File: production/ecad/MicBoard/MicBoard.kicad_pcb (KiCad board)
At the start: 2 copper layers, 50.8 x 38.1 mm, 25 parts, among them J1 Conn_01x03_Pin, J2 532610771, U2 OPA1671IDBVR

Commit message: fix drc errors
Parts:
- added TP3: TestPoint, TestPoint:TestPoint_Pad_D1.0mm, F.Cu at (77.7, 61.6)
- moved TP1 35.7 mm to (60.1, 84.7)
- moved TP2 14.4 mm to (72.4, 70.9)
- moved R3 1.43 mm to (68.1, 71.0)
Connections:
- R1 pad 2: +3.3V -> +3V3
- U2 pad 5: +3.3V -> +3V3
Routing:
- net Net-(U2-OUT): track 28.2 -> 59.6 mm
- net Net-(U2-+IN): track 13.5 -> 41.3 mm
- net GND: track 45.2 -> 54.3 mm, vias 12 -> 14
- net +3V3: track 12.9 -> 17.9 mm, vias 4 -> 5
- net +3.3V: track 2.63 -> 0.00 mm, vias 1 -> 0
- added copper zone on F.Cu, net +3V3
- added copper zone on B.Cu, net GND

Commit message: more drc fixes
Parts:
- moved TP2 8.05 mm to (64.4, 70.0)
- moved R6 7.55 mm to (72.2, 70.7), turned to 0 degrees
- moved R3 1.76 mm to (67.9, 69.2), turned to -90 degrees
- moved C2 0.25 mm to (67.5, 61.7)
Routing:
- net Net-(U2-OUT): track 59.6 -> 42.9 mm
- net Net-(U2--IN): track 38.7 -> 35.7 mm
- net Net-(C2-Pad1): track 18.8 -> 19.8 mm
- net Net-(U2-+IN): track 41.3 -> 40.3 mm

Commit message: more fixes to layout
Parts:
- moved R2 9.09 mm to (66.5, 56.2), turned to -90 degrees
- moved C10 8.74 mm to (89.9, 75.2)
- moved C9 8.74 mm to (85.3, 75.2)
- moved R6 7.87 mm to (66.6, 76.2)
- moved C2 5.62 mm to (64.3, 66.4), turned to -90 degrees
- moved TP2 4.90 mm to (68.6, 67.4), turned to 180 degrees
- moved R3 3.93 mm to (64.3, 70.8)
- moved R4 2.69 mm to (71.8, 56.2)
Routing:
- net Net-(U2-+IN): track 40.3 -> 23.5 mm
- net Net-(C1-Pad1): track 27.4 -> 17.1 mm
- net +3V3: track 17.9 -> 10.7 mm, vias 5 -> 2
- net Net-(U3-GSEL): track 11.9 -> 5.37 mm
- net Net-(U2-OUT): track 42.9 -> 47.9 mm
- net Net-(U2--IN): track 35.7 -> 38.5 mm
- net Net-(C2-Pad1): track 19.8 -> 18.0 mm
- net Net-(U3-REGO): track 7.94 -> 6.32 mm
- net GND: track 54.2 -> 54.7 mm
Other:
- outline, holes or cut-outs redrawn

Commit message: ground mounting holes
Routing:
- net GND: vias 14 -> 18
- net (no net): vias 4 -> 0
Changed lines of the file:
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@@
   (gr_circle (center 97.79 54.609998) (end 99.06 52.832)
     (stroke (width 0.1) (type default)) (fill none) (layer "Edge.Cuts"))
-  (via (at 54.61 54.61) (size 4.318) (drill 3.7973) (layers "F.Cu" "B.Cu") (net 0))
-  (via (at 97.79 54.61) (size 4.318) (drill 3.7973) (layers "F.Cu" "B.Cu") (net 0))
-  (via (at 54.61 85.09) (size 4.318) (drill 3.7973) (layers "F.Cu" "B.Cu") (net 0))
-  (via (at 97.79 85.09) (size 4.318) (drill 3.7973) (layers "F.Cu" "B.Cu") (net 0))
   (segment (start 71.708 55.278) (end 71.755 55.325) (width 0.25) (layer "F.Cu") (net 1))
   (segment (start 60.786 57.357) (end 60.786 53.467) (width 0.25) (layer "F.Cu") (net 1))
@@
   (segment (start 86.294 76.83) (end 86.294 75.184) (width 0.25) (layer "F.Cu") (net 2))
   (segment (start 55.118 80.01) (end 53.086 80.01) (width 0.25) (layer "F.Cu") (net 2))
+  (via (at 54.61 54.61) (size 4.318) (drill 3.7973) (layers "F.Cu" "B.Cu") (free) (net 2))
+  (via (at 97.79 54.61) (size 4.318) (drill 3.7973) (layers "F.Cu" "B.Cu") (free) (net 2))
   (via (at 92.837 65.278) (size 0.8) (drill 0.4) (layers "F.Cu" "B.Cu") (free) (net 2))
   (via (at 70.104 64.516) (size 0.8) (drill 0.4) (layers "F.Cu" "B.Cu") (net 2))
+  (via (at 54.61 85.09) (size 4.318) (drill 3.7973) (layers "F.Cu" "B.Cu") (free) (net 2))
   (via (at 97.155 78.486) (size 0.8) (drill 0.4) (layers "F.Cu" "B.Cu") (free) (net 2))
   (via (at 86.934 77.47) (size 0.8) (drill 0.4) (layers "F.Cu" "B.Cu") (free) (net 2))
@@
   (via (at 52.959 80.137) (size 0.8) (drill 0.4) (layers "F.Cu" "B.Cu") (free) (net 2))
   (via (at 80.137 58.547) (size 0.8) (drill 0.4) (layers "F.Cu" "B.Cu") (free) (net 2))
+  (via (at 97.79 85.09) (size 4.318) (drill 3.7973) (layers "F.Cu" "B.Cu") (free) (net 2))
   (via (at 97.409 58.674) (size 0.8) (drill 0.4) (layers "F.Cu" "B.Cu") (free) (net 2))
   (via (at 91.506 77.47) (size 0.8) (drill 0.4) (layers "F.Cu" "B.Cu") (free) (net 2))

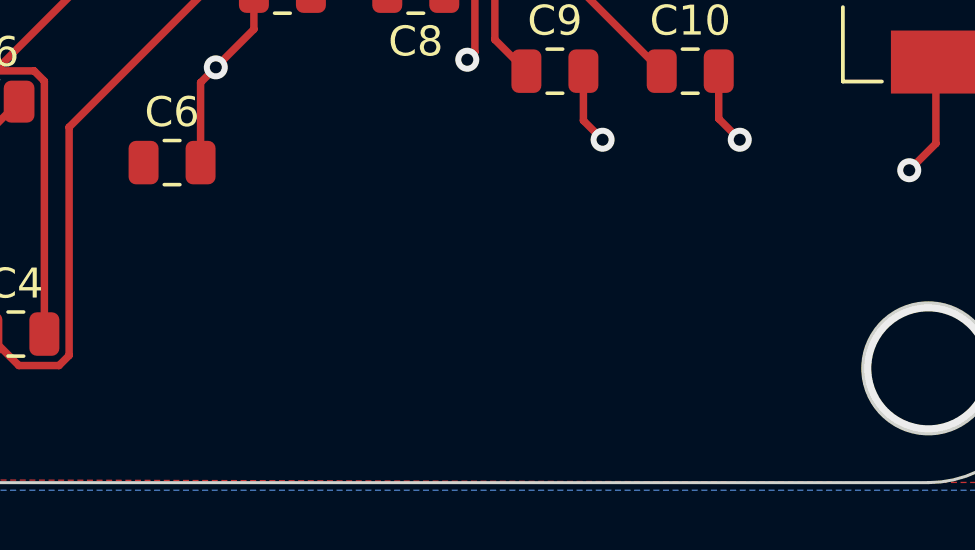
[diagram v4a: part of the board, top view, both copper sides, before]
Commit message: add turtle and fish
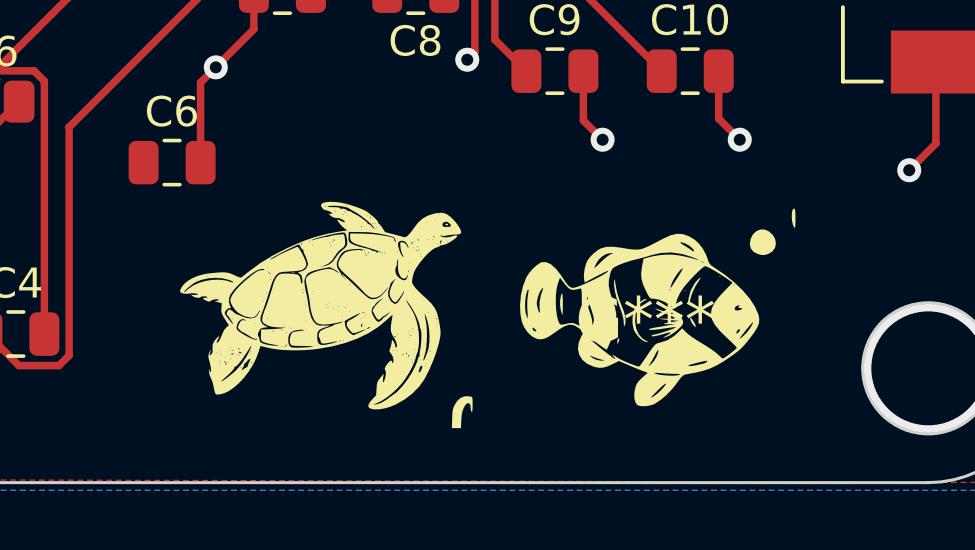
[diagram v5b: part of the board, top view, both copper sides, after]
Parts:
- added G***: LOGO, LOGO, F.Cu at (88.4, 83.5)
- added G***: LOGO, LOGO, F.Cu at (77.6, 82.9)

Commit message: rearrange stuff
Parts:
- removed TP1: TestPoint, TestPoint:TestPoint_Pad_D1.0mm
- moved C6 8.84 mm to (79.8, 73.2), turned to 180 degrees
- moved C8 4.61 mm to (79.9, 68.0)
- moved C5 3.93 mm to (79.8, 70.9), turned to 180 degrees
- moved C1 2.47 mm to (61.0, 61.5)
- moved R1 2.47 mm to (61.2, 55.9)
- moved C7 2.10 mm to (79.8, 65.5)
- moved C3 1.93 mm to (58.0, 79.8)
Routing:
- net GND: track 54.7 -> 42.7 mm, vias 18 -> 16
- net Net-(U2-OUT): track 47.9 -> 39.3 mm
- net Net-(C1-Pad1): track 17.1 -> 19.9 mm
- net Net-(C3-Pad2): track 6.77 -> 4.97 mm
